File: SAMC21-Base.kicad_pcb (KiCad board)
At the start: 4 copper layers, 28.5 x 42 mm, 63 parts, among them J1 Conn_01x04, J2 Conn_01x10, J3 Conn_01x10, J5 Conn_ARM_JTAG_SWD_10, U1 ATSAMC21E18A-AUT, U2 TJA1043T, U3 LMR50410-Q1, U4 MCP1703A, Y1 8MHz

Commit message: cleanup after review-3
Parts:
- C19, C20: value 18pF -> 33pF
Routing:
- net GND: track 65.0 -> 50.7 mm, vias 33 -> 51
- net CAN_RX: track 17.8 -> 16.6 mm
- net VDD: track 19.0 -> 17.9 mm, vias 5 -> 6
- net INH: track 57.7 -> 57.1 mm
- net CAN_L: track 26.3 -> 25.7 mm
- net +5V: vias 13 -> 16
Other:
- net class Power: via_dia 0.8 -> 0.6; via_drill 0.4 -> 0.3

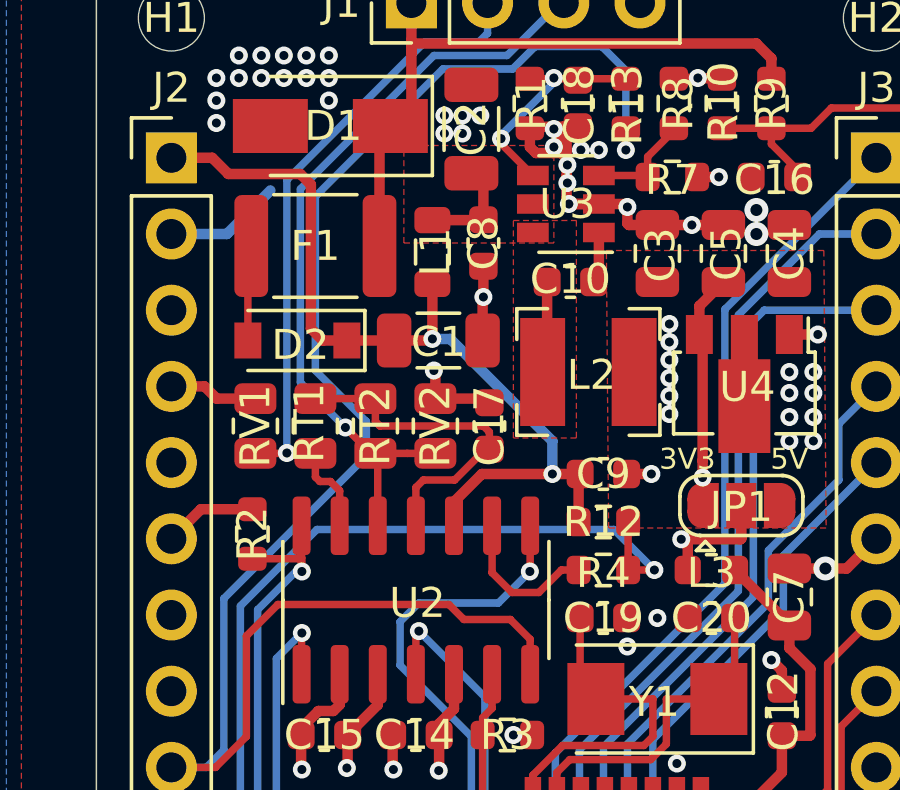
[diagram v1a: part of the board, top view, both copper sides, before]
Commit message: use DCDC_IN for TJA1043 Vbat
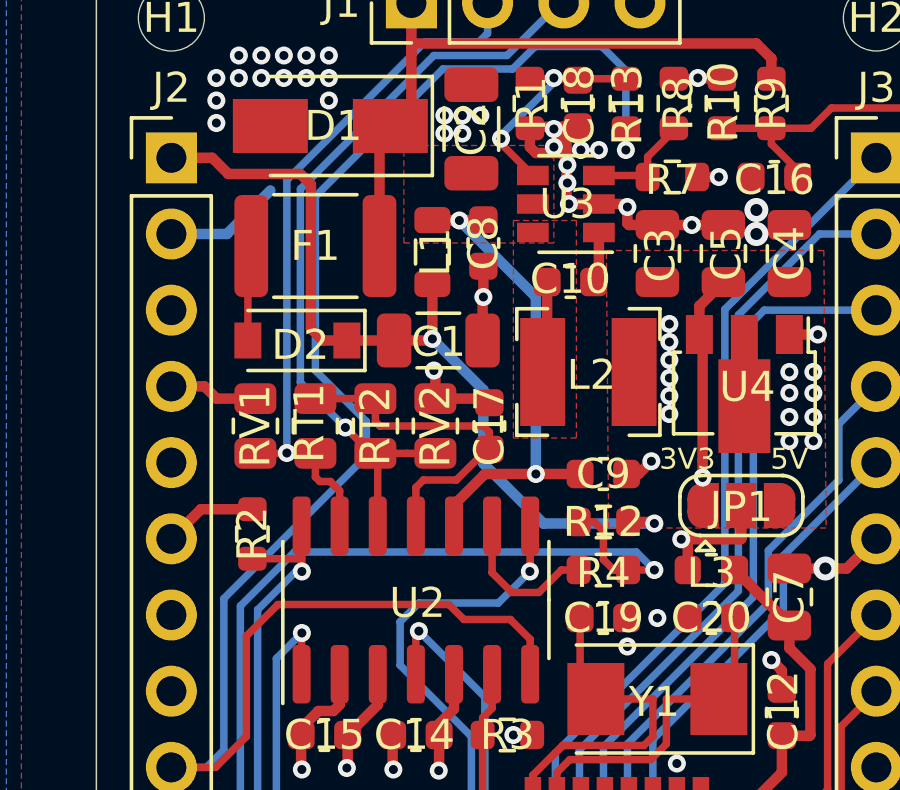
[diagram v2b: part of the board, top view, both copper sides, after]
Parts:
- turned R12 to 180 degrees
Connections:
- C9 pad 1: +36V -> /DCDC_IN
- U2 pad 10: +36V -> /DCDC_IN
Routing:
- net /DCDC_IN: track 3.42 -> 18.0 mm, vias 0 -> 2
- net +36V: track 29.5 -> 28.3 mm
- net WAKE: track 29.3 -> 30.0 mm
